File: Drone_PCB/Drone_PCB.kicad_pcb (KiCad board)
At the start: 2 copper layers, 76 x 51 mm, 63 parts, among them J1 Conn_01x04_Pin, J2 Conn_01x08_Socket, J3 Conn_01x05_Socket, J4 Conn_01x02_Socket, J5 Conn_01x02_Socket, J6 Conn_01x02_Socket, J7 Conn_01x02_Socket, J8 Conn_01x02_Socket, J9 USB_B_Micro, Q1 AO3400A, Q2 AO3400A, Q3 AO3400A, Q4 AO3400A, Q5 AO3400A, Q6 AO3400A, SW1 SW_Push, SW2 SW_SPST, U1 STM32F411RCT6, U2 AP2112K-3.3, U3 TP4056-42-ESOP8, U4 DW01A, Y1 26MHz

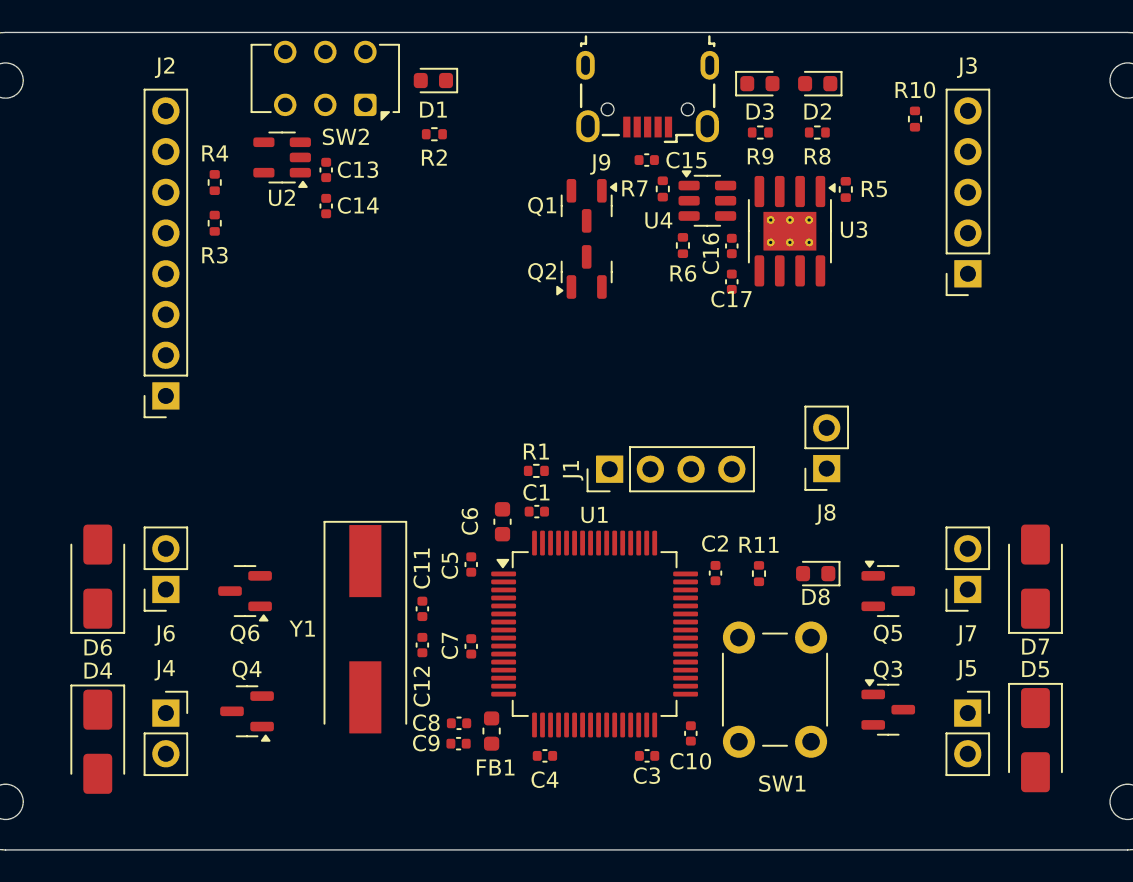
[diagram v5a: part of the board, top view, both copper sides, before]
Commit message: Created router using FreeRouting
We switched Bottom Layer to signal to enable FreeRouting
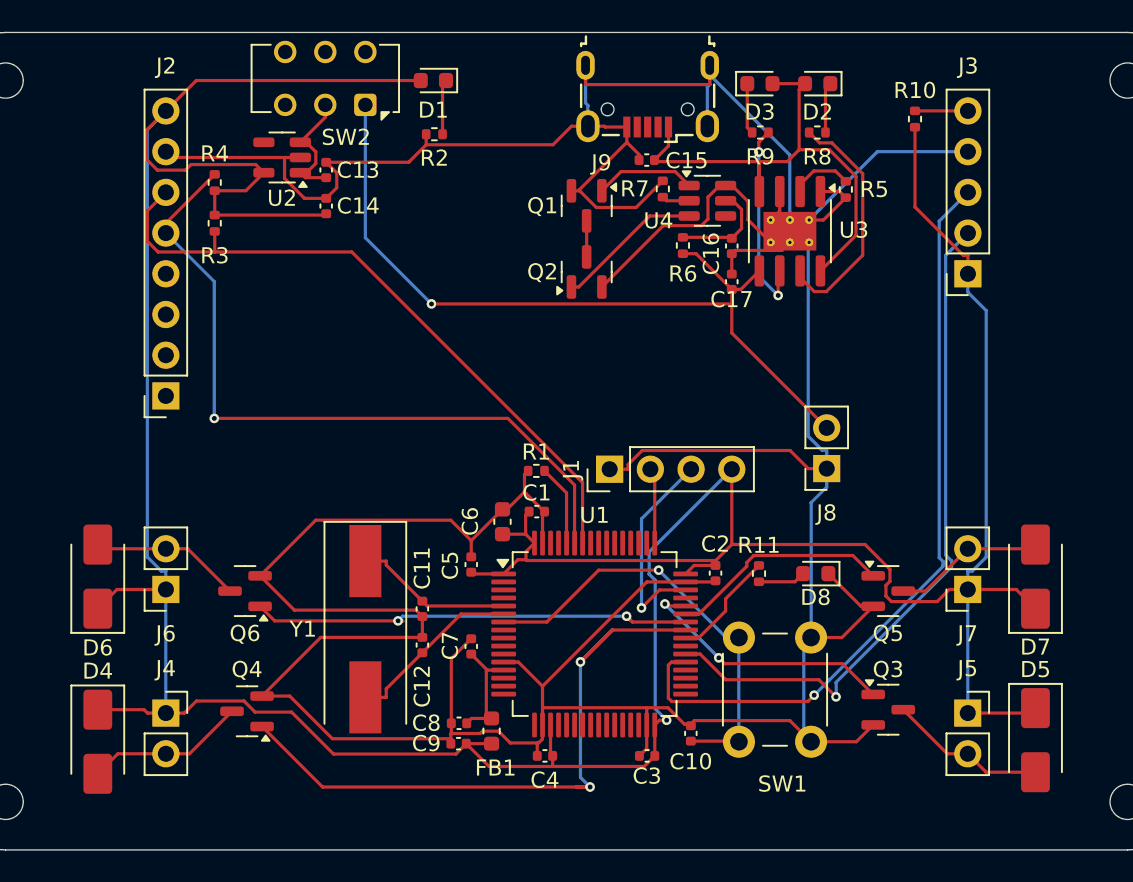
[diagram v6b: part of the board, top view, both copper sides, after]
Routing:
- net GND: track 0.00 -> 302.7 mm
- net +3.3V: track 0.00 -> 241.8 mm, vias 0 -> 1
- net /PWM_LB: track 0.00 -> 52.1 mm, vias 0 -> 2
- net /B+: track 0.00 -> 50.1 mm, vias 0 -> 1
- net /RX: track 0.00 -> 48.3 mm, vias 0 -> 1
- net /SDA: track 0.00 -> 45.6 mm, vias 0 -> 1
- net /TX: track 0.00 -> 43.1 mm, vias 0 -> 1
- net /SCL: track 0.00 -> 42.0 mm
- net VBUS: track 0.00 -> 31.0 mm
- net /PWM_LF: track 0.00 -> 29.8 mm, vias 0 -> 2
- net /NRST: track 0.00 -> 27.3 mm, vias 0 -> 1
- net /PWM_RB: track 0.00 -> 16.7 mm, vias 0 -> 2
- net /CHRG_LED: track 0.00 -> 15.1 mm
- net /PWM_RF: track 0.00 -> 13.9 mm
- net /SWDIO: track 0.00 -> 13.2 mm, vias 0 -> 1
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
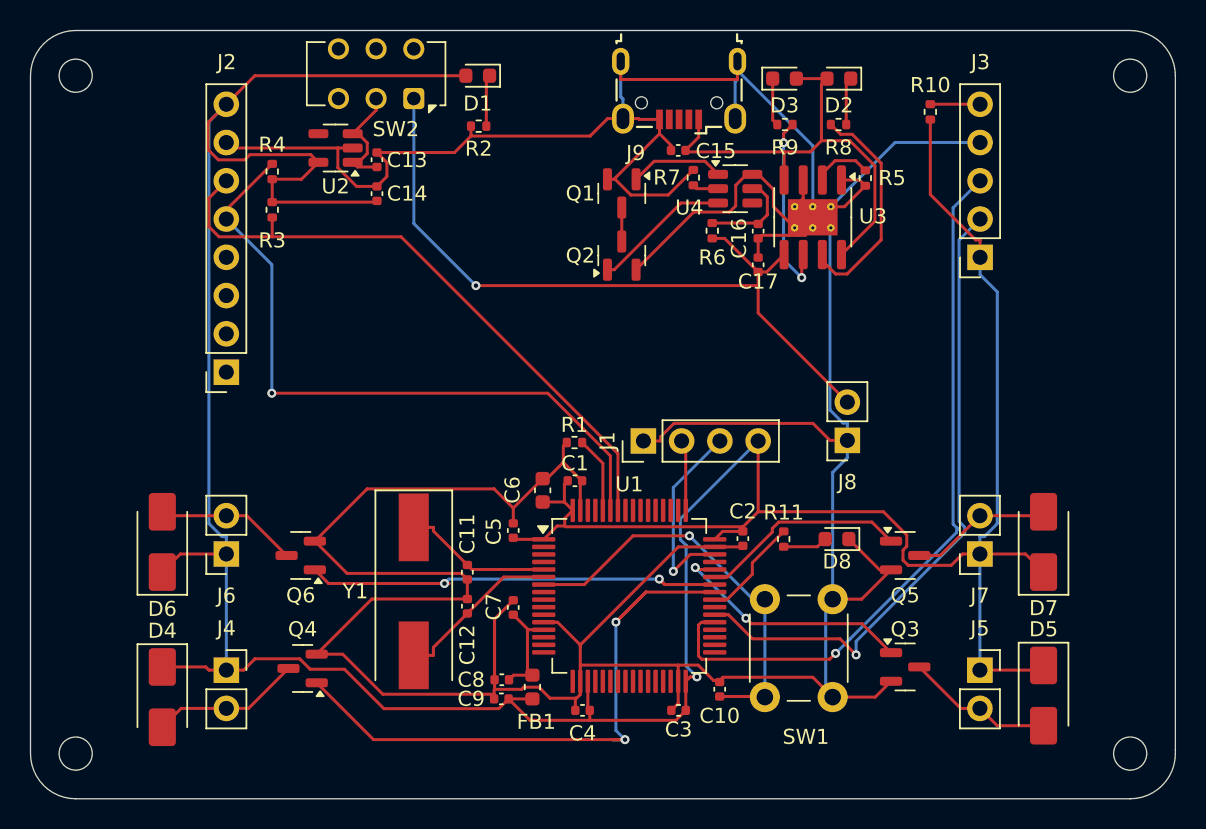
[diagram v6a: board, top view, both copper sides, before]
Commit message: Increase drill size and add silkscreen labels
Updated several pad drill sizes from 0.2mm to 0.3mm for improved manufacturability. Added silkscreen text labels for connectors and components, and updated PCB routing and backup files to reflect latest design changes.
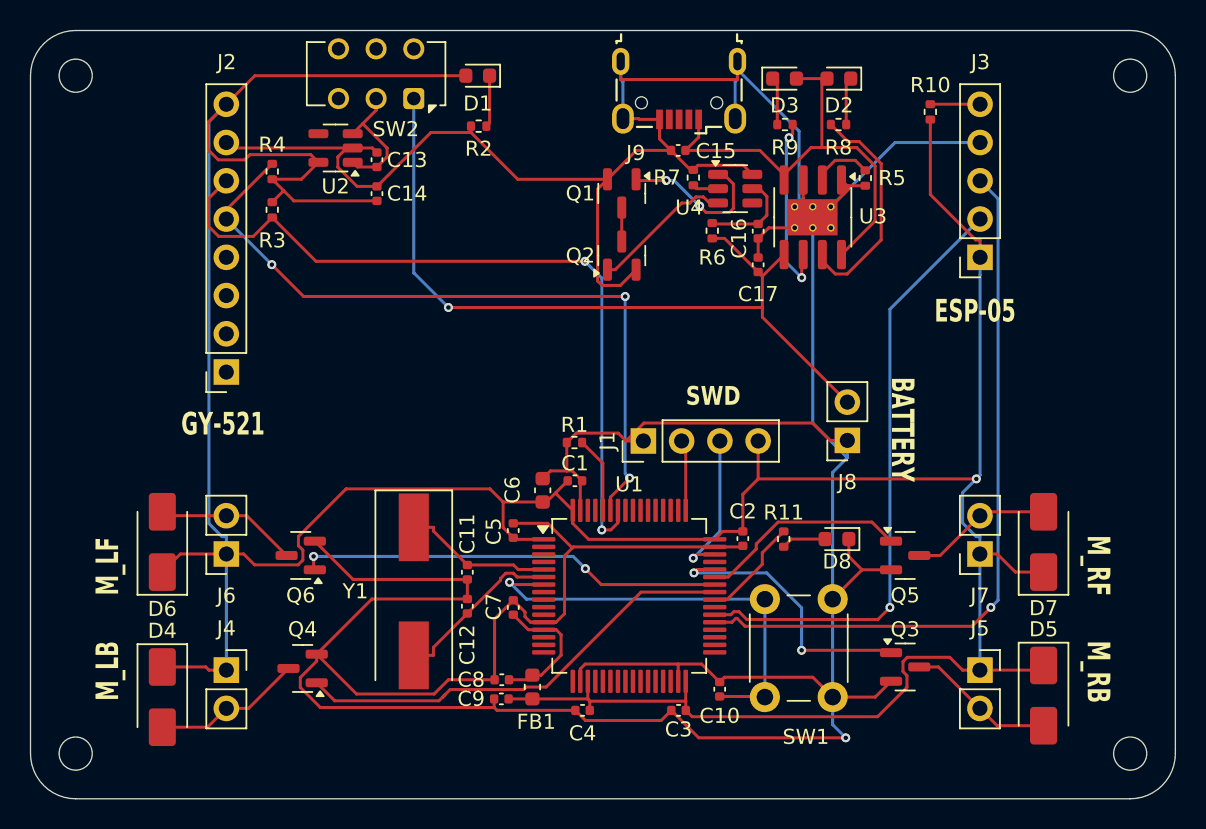
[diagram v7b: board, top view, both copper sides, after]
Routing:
- net /PWM_LB: track 52.1 -> 30.1 mm, vias 2 -> 0
- net GND: track 302.7 -> 322.7 mm, vias 0 -> 1
- net /SCL: track 42.0 -> 50.9 mm, vias 0 -> 2
- net /OD: track 6.30 -> 11.8 mm, vias 0 -> 2
- net /SWDIO: track 13.2 -> 10.0 mm
- net /SDA: track 45.6 -> 48.4 mm, vias 1 -> 3
- net /B+: track 50.1 -> 52.8 mm
- net /TX: track 43.1 -> 40.5 mm
- net +3.3VA: track 7.15 -> 9.22 mm
- net /NRST: track 27.3 -> 29.3 mm
- net /PWM_RB: track 16.7 -> 18.4 mm
- net /PWM_LF: track 29.8 -> 28.3 mm
- net /PWR: track 7.75 -> 8.54 mm
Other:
- board text added: "BATTERY"
- board text added: "ESP-05"
- board text added: "GY-521"
- board text added: "M_LB"
- board text added: "M_LF"
- board text added: "M_RB"
- board text added: "M_RF"
- board text added: "SWD"
